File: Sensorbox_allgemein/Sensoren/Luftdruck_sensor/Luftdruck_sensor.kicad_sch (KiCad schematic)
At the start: 2 parts

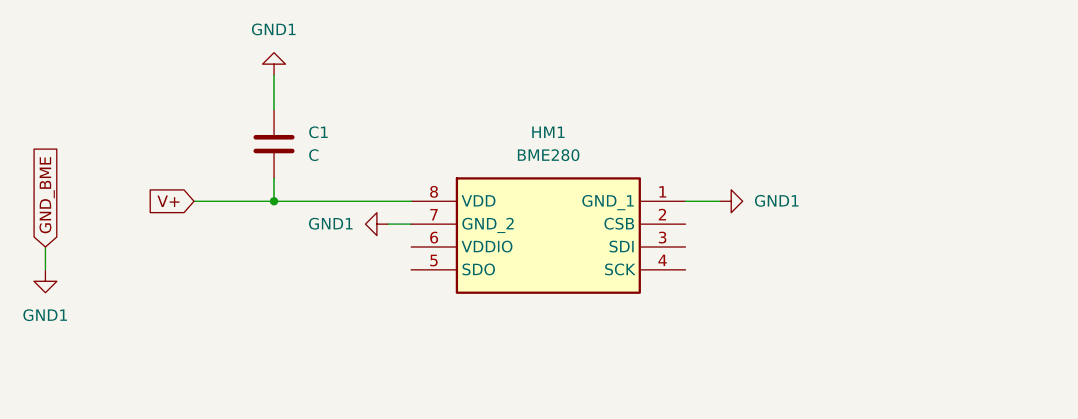
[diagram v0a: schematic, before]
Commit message: sch. neben sensoren
pins rausgesucht
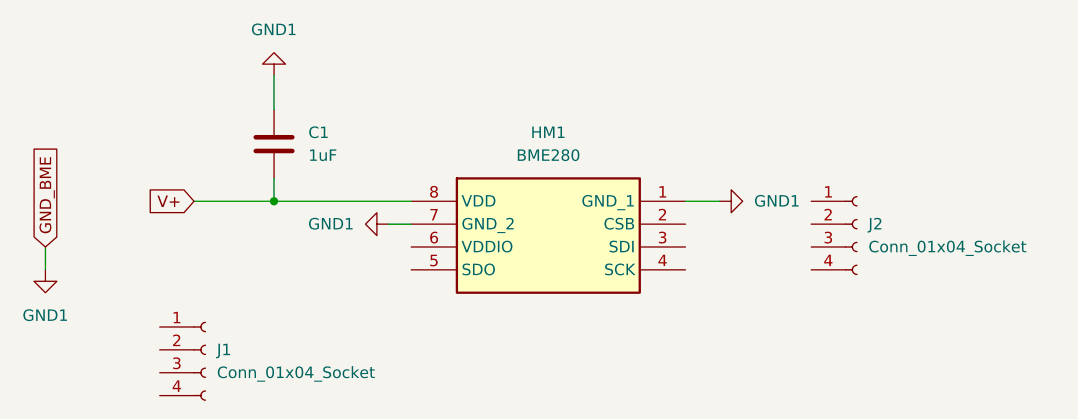
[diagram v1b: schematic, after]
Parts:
- added J1, J2: Conn_01x04_Socket, Connector_PinSocket_2.00mm:PinSocket_1x04_P2.00mm_Vertical, symbol Connector:Conn_01x04_Socket
- C1: value C -> 1uF
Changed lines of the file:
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@@
 			)
 		)
-		(property "Value" "C"
+		(property "Value" "1uF"
 			(at 124.46 64.7699 0)
 			(effects
@@
 					(unit 1)
 				)
+			)
+		)
+	)
+	(symbol
+		(lib_id "Connector:Conn_01x04_Socket")
+		(at 113.03 86.36 0)
+		(unit 1)
+		(exclude_from_sim no)
+		(in_bom yes)
+		(on_board yes)
+		(dnp no)
+		(fields_autoplaced yes)
+		(property "Reference" "J1"
+			(at 114.3 86.3599 0)
+			(effects
+				(font
+					(size 1.27 1.27)
+				)
+				(justify left)
+			)
+		)
+		(property "Value" "Conn_01x04_Socket"
+			(at 114.3 88.8999 0)
+			(effects
+				(font
+					(size 1.27 1.27)
+				)
+				(justify left)
+			)
+		)
+		(property "Footprint" "Connector_PinSocket_2.00mm:PinSocket_1x04_P2.00mm_Vertical"
+			(at 113.03 86.36 0)
+			(effects
+				(font
+					(size 1.27 1.27)
+				)
+				(hide yes)
+			)
+		)
+		(property "Datasheet" "~"
+			(at 113.03 86.36 0)
+			(effects
+				(font
+					(size 1.27 1.27)
+				)
+				(hide yes)
+			)
+		)
+		(property "Description" "Generic connector, single row, 01x04, script generated"
+			(at 113.03 86.36 0)
+			(effects
+				(font
+					(size 1.27 1.27)
+				)
+				(hide yes)
+			)
+		)
+		(pin "1"
+		)
+		(pin "2"
+		)
+		(pin "4"
+		)
+		(pin "3"
+		)
+		(instances
+			(project "Luftdruck_sensor"
+				(path "/5c0c1cac-ccf9-44ca-9405-149990707d0f"
+					(reference "J1")
+					(unit 1)
+				)
+			)
+		)
+	)
+	(symbol
+		(lib_id "Connector:Conn_01x04_Socket")
+		(at 185.42 72.39 0)
+		(unit 1)
+		(exclude_from_sim no)
+		(in_bom yes)
+		(on_board yes)
+		(dnp no)
+		(fields_autoplaced yes)
+		(property "Reference" "J2"
+			(at 186.69 72.3899 0)
+			(effects
+				(font
+					(size 1.27 1.27)
+				)
+				(justify left)
+			)
+		)
+		(property "Value" "Conn_01x04_Socket"
+			(at 186.69 74.9299 0)
+			(effects
+				(font
+					(size 1.27 1.27)
+				)
+				(justify left)
+			)
+		)
+		(property "Footprint" "Connector_PinSocket_2.00mm:PinSocket_1x04_P2.00mm_Vertical"
+			(at 185.42 72.39 0)
+			(effects
+				(font
+					(size 1.27 1.27)
+				)
+				(hide yes)
+			)
+		)
+		(property "Datasheet" "~"
+			(at 185.42 72.39 0)
+			(effects
+				(font
+					(size 1.27 1.27)
+				)
+				(hide yes)
+			)
+		)
+		(property "Description" "Generic connector, single row, 01x04, script generated"
+			(at 185.42 72.39 0)
+			(effects
+				(font
+					(size 1.27 1.27)
+				)
+				(hide yes)
+			)
+		)
+		(pin "2"
+		)
+		(pin "3"
+		)
+		(pin "1"
+		)
+		(pin "4"
+		)
+		(instances
+			(project "Luftdruck_sensor"
+				(path "/5c0c1cac-ccf9-44ca-9405-149990707d0f"
+					(reference "J2")
+					(unit 1)
+				)
